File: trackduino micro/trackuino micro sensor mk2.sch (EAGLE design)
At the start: 43 parts, among them IC2 74AHC1G125DBV, SW1 SPST_TACT-KMR2, U1 ATMEGA168MLF, Y1 16MHZ

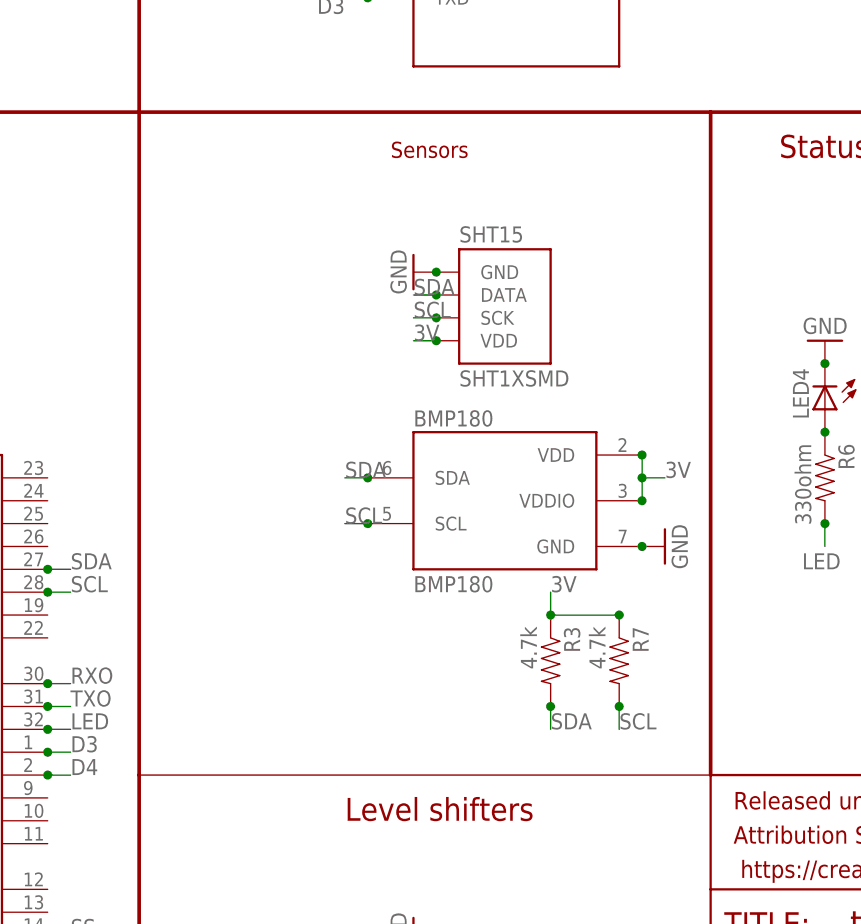
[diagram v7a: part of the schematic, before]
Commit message: replaced sht15
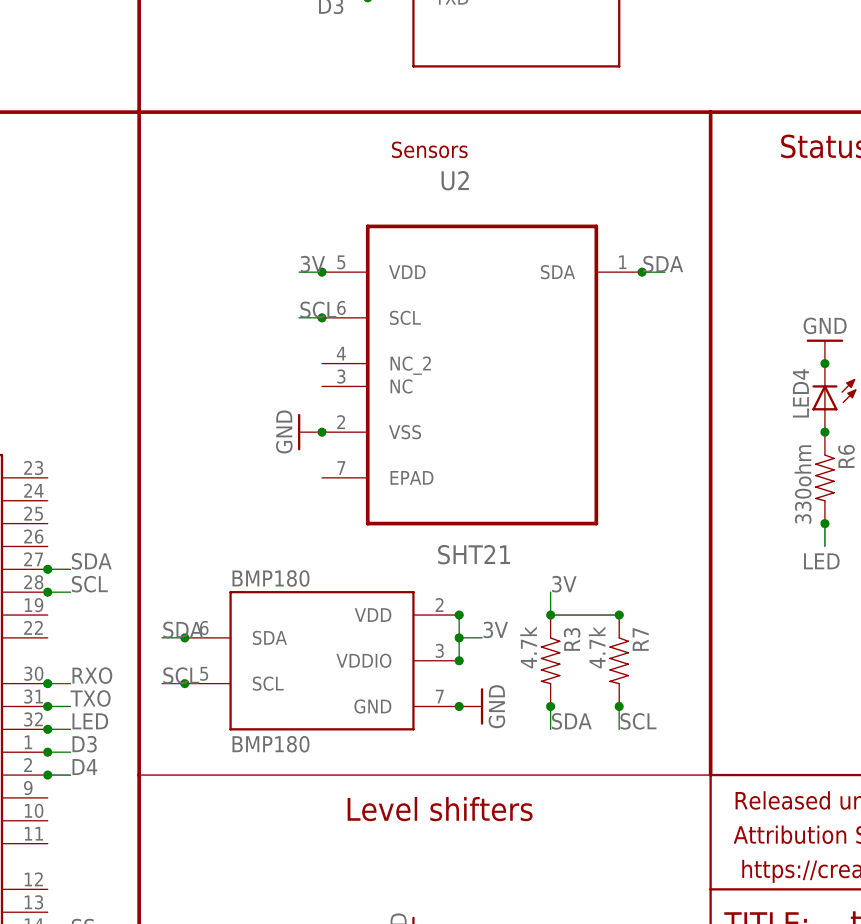
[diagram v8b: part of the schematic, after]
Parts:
- removed SHT15: SHT1XSMD, SparkFun-Sensors:SHT1XSMD
- added U2: SHT21, sht21:SHT21
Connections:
- net 3V: now also U2.VDD; no longer SHT15.VDD
- net GND: now also U2.VSS; no longer SHT15.GND
- net SCL: now also U2.SCL; no longer SHT15.SCK
- net SDA: now also U2.SDA; no longer SHT15.DATA
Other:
- moved on the sheet: BMP180
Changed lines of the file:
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@@
 <part name="RX" library="SparkFun-Connectors" deviceset="M02" device="PTH" value="RX"/>
 <part name="GND10" library="SparkFun-Aesthetics" deviceset="GND" device=""/>
-<part name="SHT15" library="SparkFun-Sensors" deviceset="SHT1X" device="SMD"/>
 <part name="BMP180" library="SparkFun-Sensors" deviceset="BMP180" device=""/>
 <part name="GND16" library="SparkFun-Aesthetics" deviceset="GND" device=""/>
@@
 <part name="C9" library="resistor" deviceset="C-US" device="C1206" value="100uf"/>
 <part name="GND31" library="SparkFun-Aesthetics" deviceset="GND" device=""/>
+<part name="U2" library="sht21" deviceset="SHT21" device=""/>
 </parts>
 <sheets>
@@
 <instance part="RX" gate="G$1" x="231.14" y="83.82"/>
 <instance part="GND10" gate="1" x="208.28" y="58.42" rot="R90"/>
-<instance part="SHT15" gate="G$1" x="124.46" y="86.36"/>
-<instance part="BMP180" gate="G$1" x="124.46" y="66.04"/>
-<instance part="GND16" gate="1" x="142.24" y="60.96" rot="R90"/>
-<instance part="GND20" gate="1" x="114.3" y="91.44" rot="R270"/>
+<instance part="BMP180" gate="G$1" x="104.14" y="48.26"/>
+<instance part="GND16" gate="1" x="121.92" y="43.18" rot="R90"/>
+<instance part="GND20" gate="1" x="101.6" y="73.66" rot="R270"/>
 <instance part="R3" gate="G$1" x="129.54" y="48.26" rot="R270"/>
 <instance part="R7" gate="G$1" x="137.16" y="48.26" rot="R270"/>
@@
 <instance part="C9" gate="G$1" x="58.42" y="137.16"/>
 <instance part="GND31" gate="1" x="58.42" y="129.54"/>
+<instance part="U2" gate="A" x="121.92" y="83.82"/>
 </instances>
 <busses>
@@
 <pinref part="BMP180" gate="G$1" pin="GND"/>
 <pinref part="GND16" gate="1" pin="GND"/>
-<junction x="139.7" y="60.96"/>
-</segment>
-<segment>
-<pinref part="SHT15" gate="G$1" pin="GND"/>
-<pinref part="GND20" gate="1" pin="GND"/>
-<junction x="116.84" y="91.44"/>
+<junction x="119.38" y="43.18"/>
 </segment>
 <segment>
@@
 <pinref part="GND31" gate="1" pin="GND"/>
 <junction x="58.42" y="132.08"/>
+</segment>
+<segment>
+<pinref part="U2" gate="A" pin="VSS"/>
+<pinref part="GND20" gate="1" pin="GND"/>
+<junction x="104.14" y="73.66"/>
 </segment>
 </net>
@@
 <pinref part="BMP180" gate="G$1" pin="VDD"/>
 <pinref part="BMP180" gate="G$1" pin="VDDIO"/>
-<wire x1="139.7" y1="71.12" x2="139.7" y2="68.58" width="0.1524" layer="91"/>
-<wire x1="139.7" y1="68.58" x2="139.7" y2="66.04" width="0.1524" layer="91"/>
-<wire x1="139.7" y1="68.58" x2="142.24" y2="68.58" width="0.1524" layer="91"/>
-<junction x="139.7" y="71.12"/>
-<junction x="139.7" y="66.04"/>
-<junction x="139.7" y="68.58"/>
-<label x="142.24" y="68.58" size="1.778" layer="95"/>
-</segment>
-<segment>
-<pinref part="SHT15" gate="G$1" pin="VDD"/>
-<wire x1="116.84" y1="83.82" x2="114.3" y2="83.82" width="0.1524" layer="91"/>
-<junction x="116.84" y="83.82"/>
-<label x="114.3" y="83.82" size="1.778" layer="95"/>
+<wire x1="119.38" y1="53.34" x2="119.38" y2="50.8" width="0.1524" layer="91"/>
+<wire x1="119.38" y1="50.8" x2="119.38" y2="48.26" width="0.1524" layer="91"/>
+<wire x1="119.38" y1="50.8" x2="121.92" y2="50.8" width="0.1524" layer="91"/>
+<junction x="119.38" y="53.34"/>
+<junction x="119.38" y="48.26"/>
+<junction x="119.38" y="50.8"/>
+<label x="121.92" y="50.8" size="1.778" layer="95"/>
+</segment>
+<segment>
+<wire x1="104.14" y1="91.44" x2="101.6" y2="91.44" width="0.1524" layer="91"/>
+<label x="101.6" y="91.44" size="1.778" layer="95"/>
+<pinref part="U2" gate="A" pin="VDD"/>
+<junction x="104.14" y="91.44"/>
 </segment>
 <segment>
@@
 </segment>
 <segment>
-<pinref part="SHT15" gate="G$1" pin="DATA"/>
-<wire x1="116.84" y1="88.9" x2="114.3" y2="88.9" width="0.1524" layer="91"/>
-<label x="114.3" y="88.9" size="1.778" layer="95"/>
-<junction x="116.84" y="88.9"/>
+<wire x1="142.24" y1="91.44" x2="139.7" y2="91.44" width="0.1524" layer="91"/>
+<label x="139.7" y="91.44" size="1.778" layer="95"/>
+<pinref part="U2" gate="A" pin="SDA"/>
+<junction x="139.7" y="91.44"/>
 </segment>
 <segment>
 <pinref part="BMP180" gate="G$1" pin="SDA"/>
-<wire x1="109.22" y1="68.58" x2="106.68" y2="68.58" width="0.1524" layer="91"/>
-<label x="106.68" y="68.58" size="1.778" layer="95"/>
-<junction x="109.22" y="68.58"/>
+<wire x1="88.9" y1="50.8" x2="86.36" y2="50.8" width="0.1524" layer="91"/>
+<label x="86.36" y="50.8" size="1.778" layer="95"/>
+<junction x="88.9" y="50.8"/>
 </segment>
 <segment>
@@
 </segment>
 <segment>
-<pinref part="SHT15" gate="G$1" pin="SCK"/>
-<wire x1="116.84" y1="86.36" x2="114.3" y2="86.36" width="0.1524" layer="91"/>
-<label x="114.3" y="86.36" size="1.778" layer="95"/>
-<junction x="116.84" y="86.36"/>
+<wire x1="104.14" y1="86.36" x2="101.6" y2="86.36" width="0.1524" layer="91"/>
+<label x="101.6" y="86.36" size="1.778" layer="95"/>
+<pinref part="U2" gate="A" pin="SCL"/>
+<junction x="104.14" y="86.36"/>
 </segment>
 <segment>
 <pinref part="BMP180" gate="G$1" pin="SCL"/>
-<wire x1="109.22" y1="63.5" x2="106.68" y2="63.5" width="0.1524" layer="91"/>
-<label x="106.68" y="63.5" size="1.778" layer="95"/>
-<junction x="109.22" y="63.5"/>
-</segment>
-<segment>
+<wire x1="88.9" y1="45.72" x2="86.36" y2="45.72" width="0.1524" layer="91"/>
+<label x="86.36" y="45.72" size="1.778" layer="95"/>
+<junction x="88.9" y="45.72"/>
+</segment>
+<segment>
